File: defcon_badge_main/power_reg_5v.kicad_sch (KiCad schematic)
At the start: 6 parts, among them U2 TPS61023DRLR

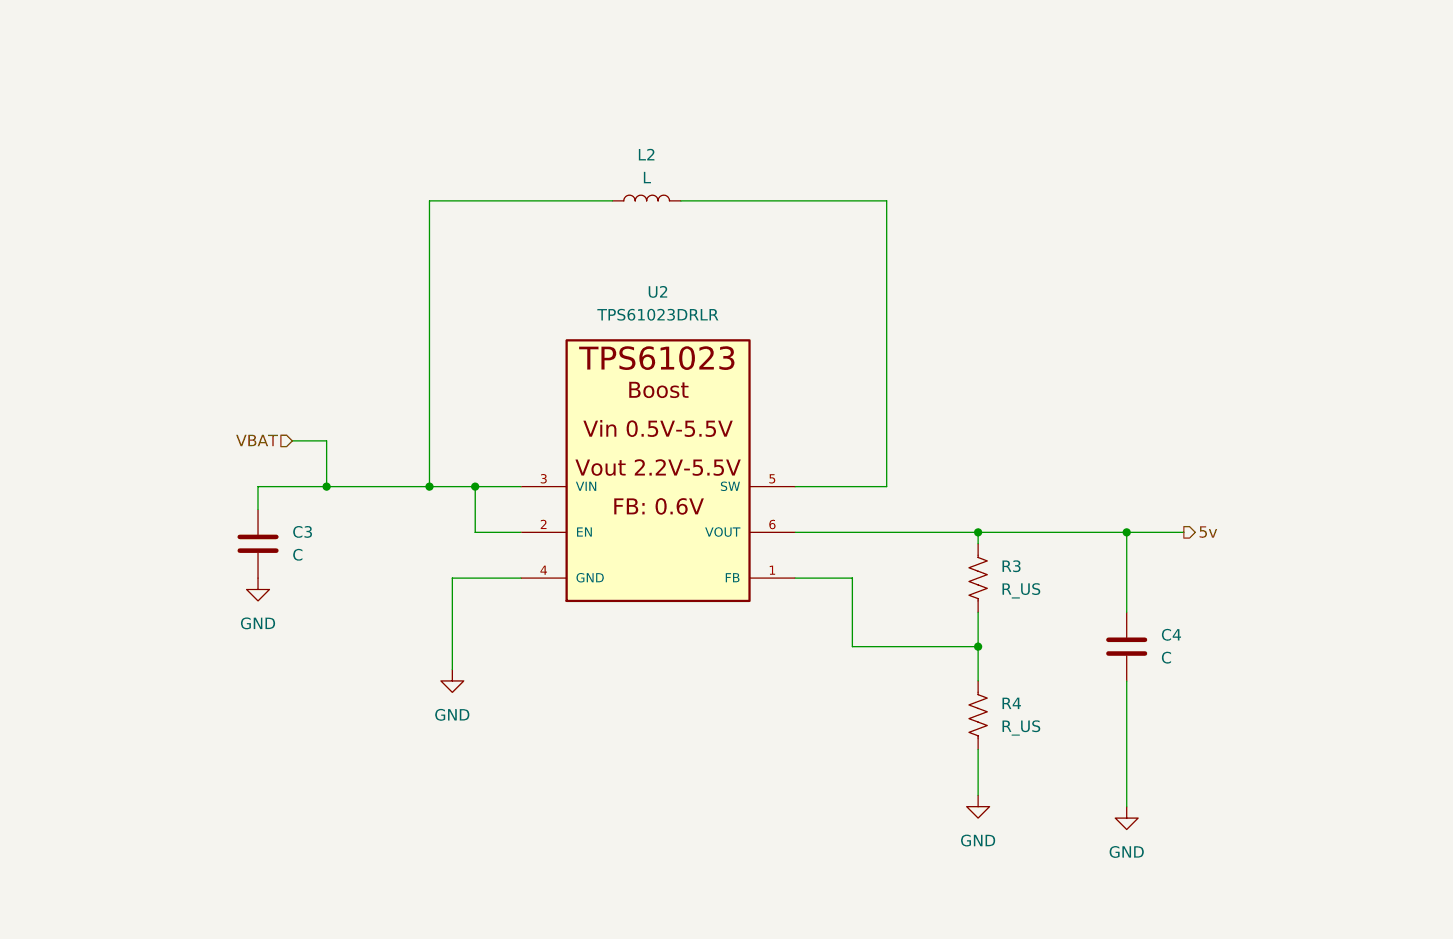
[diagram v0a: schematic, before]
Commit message: ESP32 test board layout
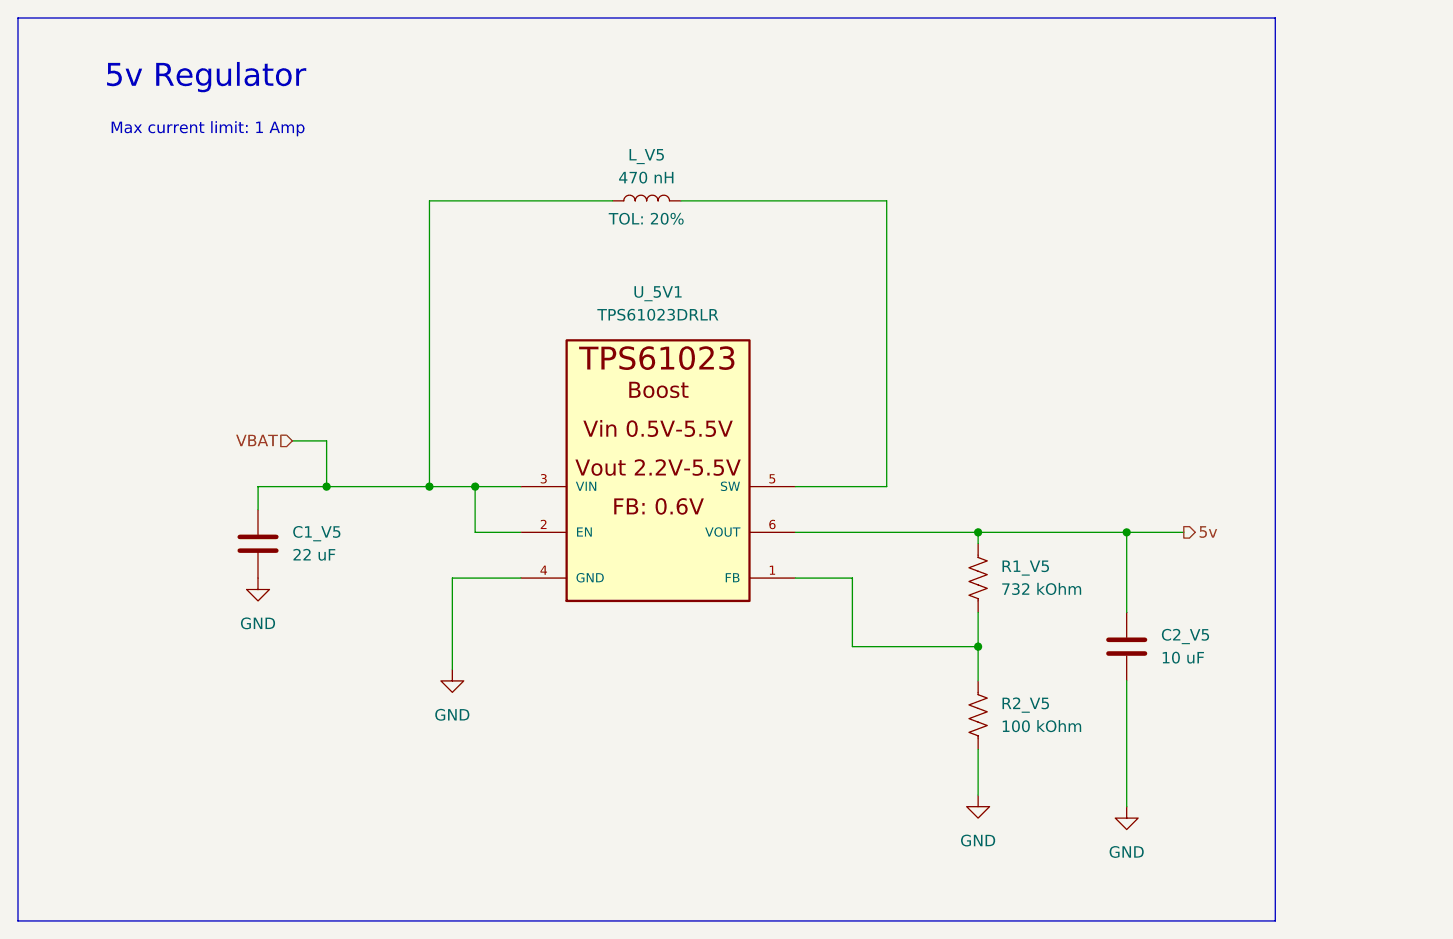
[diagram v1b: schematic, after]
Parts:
- removed L2: L, symbol Device:L
- removed U2: TPS61023DRLR, TPS61023DRLR:SOT563-ORI, symbol TPS61023DRLR:TPS61023DRLR
- added L_V5: 470 nH, Inductor_SMD:L_Neosid_SMS-ME3010, symbol Device:L
- added U_5V1: TPS61023DRLR, TPS61023DRLR:SOT563-ORI, symbol TPS61023DRLR:TPS61023DRLR
- C1_V5: renamed from C3; value C -> 22 uF; footprint (none) -> PCM_SparkFun-Coil:0805
- C2_V5: renamed from C4; value C -> 10 uF; footprint (none) -> PCM_SparkFun-Coil:0805
- R1_V5: renamed from R3; value R_US -> 732 kOhm; footprint (none) -> PCM_SparkFun-Fuse:1206
- R2_V5: renamed from R4; value R_US -> 100 kOhm; footprint (none) -> PCM_SparkFun-Fuse:1206
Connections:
- net 5v: now also U_5V1.6 (VOUT)
- net GND: now also U_5V1.4 (GND)
- net VBAT: now also L_V5.1, U_5V1.2 (EN), U_5V1.3 (VIN)
- net at R1_V5.2, R2_V5.1: now also U_5V1.1 (FB)
- new net: L_V5.2, U_5V1.5 (SW)
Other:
- note added: "5v Regulator"
- note added: "Max current limit: 1 Amp"
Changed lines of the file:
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@@
 	(generator_version "9.0")
 	(paper "A4")
+	(rectangle
+		(start 46.99 29.21)
+		(end 186.69 129.54)
+		(stroke
+			(width 0)
+			(type default)
+		)
+		(fill
+			(type none)
+		)
+	)
+	(text "Max current limit: 1 Amp"
+		(exclude_from_sim no)
+		(at 68.072 41.656 0)
+		(effects
+			(font
+				(size 1.27 1.27)
+			)
+		)
+	)
+	(text "5v Regulator"
+		(exclude_from_sim no)
+		(at 67.818 35.814 0)
+		(effects
+			(font
+				(size 2.54 2.54)
+			)
+		)
+	)
 	(junction
 		(at 97.79 81.28)
@@
 		(dnp no)
 		(fields_autoplaced yes)
-		(property "Reference" "C3"
+		(property "Reference" "C1_V5"
 			(at 77.47 86.3599 0)
 			(effects
@@
 			)
 		)
-		(property "Value" "C"
+		(property "Value" "22 uF"
 			(at 77.47 88.8999 0)
 			(effects
@@
 			)
 		)
-		(property "Footprint" ""
+		(property "Footprint" "PCM_SparkFun-Coil:0805"
 			(at 74.6252 91.44 0)
 			(effects
@@
 			(project "defcon_badge_main"
 				(path "/b497f1e3-23b9-4176-bc4d-bc3995ba532c/5a5d7d00-ae35-4e4f-8d3e-dea7a6dc9222"
-					(reference "C3")
+					(reference "C1_V5")
 					(unit 1)
 				)
@@
 		(dnp no)
 		(fields_autoplaced yes)
-		(property "Reference" "C4"
+		(property "Reference" "C2_V5"
 			(at 173.99 97.7899 0)
 			(effects
@@
 			)
 		)
-		(property "Value" "C"
+		(property "Value" "10 uF"
 			(at 173.99 100.3299 0)
 			(effects
@@
 			)
 		)
-		(property "Footprint" ""
+		(property "Footprint" "PCM_SparkFun-Coil:0805"
 			(at 171.1452 102.87 0)
 			(effects
@@
 			(project "defcon_badge_main"
 				(path "/b497f1e3-23b9-4176-bc4d-bc3995ba532c/5a5d7d00-ae35-4e4f-8d3e-dea7a6dc9222"
-					(reference "C4")
+					(reference "C2_V5")
 					(unit 1)
 				)
@@
 		(on_board yes)
 		(dnp no)
-		(fields_autoplaced yes)
-		(property "Reference" "L2"
+		(property "Reference" "L_V5"
 			(at 116.84 44.45 90)
 			(effects
@@
 			)
 		)
-		(property "Value" "L"
+		(property "Value" "470 nH"
 			(at 116.84 46.99 90)
 			(effects
@@
 			)
 		)
-		(property "Footprint" ""
+		(property "Footprint" "Inductor_SMD:L_Neosid_SMS-ME3010"
 			(at 116.84 49.53 0)
 			(effects
@@
 				)
 				(hide yes)
+			)
+		)
+		(property "PN" "74479288147"
+			(at 116.84 49.53 90)
+			(effects
+				(font
+					(size 1.27 1.27)
+				)
+				(hide yes)
+			)
+		)
+		(property "TOL" "20%"
+			(at 116.84 51.562 90)
+			(show_name yes)
+			(effects
+				(font
+					(size 1.27 1.27)
+				)
 			)
 		)
@@
 			(project "defcon_badge_main"
 				(path "/b497f1e3-23b9-4176-bc4d-bc3995ba532c/5a5d7d00-ae35-4e4f-8d3e-dea7a6dc9222"
-					(reference "L2")
+					(reference "L_V5")
 					(unit 1)
 				)
@@
 		(dnp no)
 		(fields_autoplaced yes)
-		(property "Reference" "R4"
+		(property "Reference" "R2_V5"
 			(at 156.21 105.4099 0)
 			(effects
@@
 			)
 		)
-		(property "Value" "R_US"
+		(property "Value" "100 kOhm"
 			(at 156.21 107.9499 0)
 			(effects
@@
 			)
 		)
-		(property "Footprint" ""
+		(property "Footprint" "PCM_SparkFun-Fuse:1206"
 			(at 154.686 106.934 90)
 			(effects
@@
 			(project "defcon_badge_main"
 				(path "/b497f1e3-23b9-4176-bc4d-bc3995ba532c/5a5d7d00-ae35-4e4f-8d3e-dea7a6dc9222"
-					(reference "R4")
+					(reference "R2_V5")
 					(unit 1)
 				)
@@
 		(dnp no)
 		(fields_autoplaced yes)
-		(property "Reference" "R3"
+		(property "Reference" "R1_V5"
 			(at 156.21 90.1699 0)
 			(effects
@@
 			)
 		)
-		(property "Value" "R_US"
+		(property "Value" "732 kOhm"
 			(at 156.21 92.7099 0)
 			(effects
@@
 			)
 		)
-		(property "Footprint" ""
+		(property "Footprint" "PCM_SparkFun-Fuse:1206"
 			(at 154.686 91.694 90)
 			(effects
@@
 			(project "defcon_badge_main"
 				(path "/b497f1e3-23b9-4176-bc4d-bc3995ba532c/5a5d7d00-ae35-4e4f-8d3e-dea7a6dc9222"
-					(reference "R3")
+					(reference "R1_V5")
 					(unit 1)
 				)
@@
 		(dnp no)
 		(fields_autoplaced yes)
-		(property "Reference" "U2"
+		(property "Reference" "U_5V1"
 			(at 118.11 59.69 0)
 			(effects
@@
 			)
 		)
+		(pin "2"
+		)
+		(pin "5"
+		)
 		(pin "4"
 		)
-		(pin "5"
-		)
 		(pin "6"
 		)
-		(pin "2"
-		)
 		(pin "1"
 		)
@@
 		)
 		(instances
-			(project "defcon_badge_main"
+			(project ""
 				(path "/b497f1e3-23b9-4176-bc4d-bc3995ba532c/5a5d7d00-ae35-4e4f-8d3e-dea7a6dc9222"
-					(reference "U2")
+					(reference "U_5V1")
 					(unit 1)
 				)

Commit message: more layout
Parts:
- C1_V5, C2_V5: footprint PCM_SparkFun-Coil:0805 -> joystick:R_0805_2012Metric_Pad1.20x1.40mm_HandSolder_MINE
- R1_V5, R2_V5: footprint PCM_SparkFun-Fuse:1206 -> joystick:R_1206_3216Metric_Pad1.30x1.75mm_HandSolder_MINE
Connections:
- net 5v_SW: now reaches L_V5.2, U_5V1.5 (SW)
- net 5v_FB: now reaches R1_V5.2, R2_V5.1, U_5V1.1 (FB)
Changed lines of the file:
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@@
+		)
+	)
+	(label "5v_SW"
+		(at 143.51 73.66 0)
+		(effects
+			(font
+				(size 1.27 1.27)
+			)
+			(justify left bottom)
+		)
+	)
+	(label "5v_FB"
+		(at 143.51 99.06 0)
+		(effects
+			(font
+				(size 1.27 1.27)
+			)
+			(justify left bottom)
 		)
 	)
@@
 			)
 		)
-		(property "Footprint" "PCM_SparkFun-Coil:0805"
+		(property "Footprint" "joystick:R_0805_2012Metric_Pad1.20x1.40mm_HandSolder_MINE"
 			(at 74.6252 91.44 0)
 			(effects
@@
 			)
 		)
-		(property "Footprint" "PCM_SparkFun-Coil:0805"
+		(property "Footprint" "joystick:R_0805_2012Metric_Pad1.20x1.40mm_HandSolder_MINE"
 			(at 171.1452 102.87 0)
 			(effects
@@
 			)
 		)
-		(property "Footprint" "PCM_SparkFun-Fuse:1206"
+		(property "Footprint" "joystick:R_1206_3216Metric_Pad1.30x1.75mm_HandSolder_MINE"
 			(at 154.686 106.934 90)
 			(effects
@@
 			)
 		)
-		(property "Footprint" "PCM_SparkFun-Fuse:1206"
+		(property "Footprint" "joystick:R_1206_3216Metric_Pad1.30x1.75mm_HandSolder_MINE"
 			(at 154.686 91.694 90)
 			(effects

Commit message: moar layout
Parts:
- added D_8V2: SS24FL, SS24FL:SODFL3617X108N, symbol SS24FL:SS24FL
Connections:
- net 5v: now also D_8V2.C; no longer C2_V5.1, R1_V5.1, U_5V1.6 (VOUT)
- new net 5v_out: C2_V5.1, D_8V2.A, R1_V5.1, U_5V1.6 (VOUT)
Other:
- note added: "Need to prevent USB 5v Power current backflow when connected to host"
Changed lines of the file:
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@@
 	(rectangle
 		(start 46.99 29.21)
-		(end 186.69 129.54)
+		(end 204.47 129.54)
 		(stroke
 			(width 0)
@@
 		)
 	)
+	(text "Need to prevent USB 5v Power \ncurrent backflow when connected to host"
+		(exclude_from_sim no)
+		(at 172.466 55.118 0)
+		(effects
+			(font
+				(size 1.27 1.27)
+			)
+		)
+	)
 	(text "5v Regulator"
 		(exclude_from_sim no)
@@
 		)
 	)
-	(hierarchical_label "5v"
-		(shape output)
-		(at 176.53 86.36 0)
+	(label "5v_out"
+		(at 157.48 86.36 0)
 		(effects
 			(font
 				(size 1.27 1.27)
 			)
-			(justify left)
+			(justify left bottom)
 		)
 	)
@@
 			)
 			(justify right)
+		)
+	)
+	(hierarchical_label "5v"
+		(shape output)
+		(at 186.69 86.36 0)
+		(effects
+			(font
+				(size 1.27 1.27)
+			)
+			(justify left)
 		)
 	)
@@
 					(unit 1)
 				)
+			)
+		)
+	)
+	(symbol
+		(lib_id "SS24FL:SS24FL")
+		(at 181.61 86.36 0)
+		(unit 1)
+		(exclude_from_sim no)
+		(in_bom yes)
+		(on_board yes)
+		(dnp no)
+		(fields_autoplaced yes)
+		(property "Reference" "D_8V2"
+			(at 181.61 80.01 0)
+			(effects
+				(font
+					(size 1.27 1.27)
+				)
+			)
+		)
+		(property "Value" "SS24FL"
+			(at 181.61 82.55 0)
+			(effects
+				(font
+					(size 1.27 1.27)
+				)
+			)
+		)
+		(property "Footprint" "SS24FL:SODFL3617X108N"
+			(at 181.61 86.36 0)
+			(effects
+				(font
+					(size 1.27 1.27)
+				)
+				(justify bottom)
+				(hide yes)
+			)
+		)
+		(property "Datasheet" ""
+			(at 181.61 86.36 0)
+			(effects
+				(font
+					(size 1.27 1.27)
+				)
+				(hide yes)
+			)
+		)
+		(property "Description" ""
+			(at 181.61 86.36 0)
+			(effects
+				(font
+					(size 1.27 1.27)
+				)
+				(hide yes)
+			)
+		)
+		(property "MF" "ON Semiconductor"
+			(at 181.61 86.36 0)
+			(effects
+				(font
+					(size 1.27 1.27)
+				)
+				(justify bottom)
+				(hide yes)
+			)
+		)
+		(property "MAXIMUM_PACKAGE_HEIGHT" "1.08mm"
+			(at 181.61 86.36 0)
+			(effects
+				(font
+					(size 1.27 1.27)
+				)
+				(justify bottom)
+				(hide yes)
+			)
+		)
+		(property "Package" "SOD-123F ON Semiconductor"
+			(at 181.61 86.36 0)
+			(effects
+				(font
+					(size 1.27 1.27)
+				)
+				(justify bottom)
+				(hide yes)
+			)
+		)
+		(property "Price" "None"
+			(at 181.61 86.36 0)
+			(effects
+				(font
+					(size 1.27 1.27)
+				)
+				(justify bottom)
+				(hide yes)
+			)
+		)
+		(property "Check_prices" "https://www.snapeda.com/parts/SS24FL/Onsemi/view-part/?ref=eda"
+			(at 181.61 86.36 0)
+			(effects
+				(font
+					(size 1.27 1.27)
+				)
+				(justify bottom)
+				(hide yes)
+			)
+		)
+		(property "STANDARD" "IPC-7351B"
+			(at 181.61 86.36 0)
+			(effects
+				(font
+					(size 1.27 1.27)
+				)
+				(justify bottom)
+				(hide yes)
+			)
+		)
+		(property "PARTREV" "A"
+			(at 181.61 86.36 0)
+			(effects
+				(font
+					(size 1.27 1.27)
+				)
+				(justify bottom)
+				(hide yes)
+			)
+		)
+		(property "SnapEDA_Link" "https://www.snapeda.com/parts/SS24FL/Onsemi/view-part/?ref=snap"
+			(at 181.61 86.36 0)
+			(effects
+				(font
+					(size 1.27 1.27)
+				)
+				(justify bottom)
+				(hide yes)
+			)
+		)
+		(property "MP" "SS24FL"
+			(at 181.61 86.36 0)
+			(effects
+				(font
+					(size 1.27 1.27)
+				)
+				(justify bottom)
+				(hide yes)
+			)
+		)
+		(property "Description_1" "Diode Schottky 40 V 2A Surface Mount SOD-123F"
+			(at 181.61 86.36 0)
+			(effects
+				(font
+					(size 1.27 1.27)
+				)
+				(justify bottom)
+				(hide yes)
+			)
+		)
+		(property "Availability" "In Stock"
+			(at 181.61 86.36 0)
+			(effects
+				(font
+					(size 1.27 1.27)
+				)
+				(justify bottom)
+				(hide yes)
+			)
+		)
+		(property "MANUFACTURER" "ON Semiconductor"
+			(at 181.61 86.36 0)
+			(effects
+				(font
+					(size 1.27 1.27)
+				)
+				(justify bottom)
+				(hide yes)
+			)
+		)
+		(pin "C"
+		)
+		(pin "A"
+		)
+		(instances
+			(project "defcon_badge_main"
+				(path "/b497f1e3-23b9-4176-bc4d-bc3995ba532c/5a5d7d00-ae35-4e4f-8d3e-dea7a6dc9222"
+					(reference "D_8V2")
+					(unit 1)
+				)

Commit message: added component parts and modifications
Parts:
- C1_V5: MPN (none) -> GMC21X5R226K16NT; Rating (none) -> 16V
- C2_V5: MPN (none) -> GMC21X5R106K16NT; Rating (none) -> 16V
- D_8V2: MPN (none) -> SS24FL
- L_V5: MPN (none) -> 74479288147
- R1_V5: MPN (none) -> RM12F7323CT; TOL (none) -> 1%
- R2_V5: MPN (none) -> RM12F1003CT; TOL (none) -> 1%
- U_5V1: MPN (none) -> TPS61023DRLR
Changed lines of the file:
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@@
 			)
 		)
-		(property "Datasheet" "~"
+		(property "Datasheet" "~https://calchip.com/wp-content/uploads/2025/05/GMC-Series-3.pdf"
 			(at 73.66 87.63 0)
 			(effects
@@
 		)
 		(property "Description" "Unpolarized capacitor"
+			(at 73.66 87.63 0)
+			(effects
+				(font
+					(size 1.27 1.27)
+				)
+				(hide yes)
+			)
+		)
+		(property "MPN" "GMC21X5R226K16NT"
+			(at 73.66 87.63 0)
+			(effects
+				(font
+					(size 1.27 1.27)
+				)
+				(hide yes)
+			)
+		)
+		(property "Rating" "16V"
 			(at 73.66 87.63 0)
 			(effects
@@
 			)
 		)
-		(property "Datasheet" "~"
+		(property "Datasheet" "https://calchip.com/wp-content/uploads/2025/05/GMC-Series-3.pdf"
 			(at 170.18 99.06 0)
 			(effects
@@
 		)
 		(property "Description" "Unpolarized capacitor"
+			(at 170.18 99.06 0)
+			(effects
+				(font
+					(size 1.27 1.27)
+				)
+				(hide yes)
+			)
+		)
+		(property "MPN" "GMC21X5R106K16NT"
+			(at 170.18 99.06 0)
+			(effects
+				(font
+					(size 1.27 1.27)
+				)
+				(hide yes)
+			)
+		)
+		(property "Rating" "16V"
 			(at 170.18 99.06 0)
 			(effects
@@
 			)
 		)
-		(property "Datasheet" "~"
+		(property "Datasheet" "https://www.we-online.com/components/products/datasheet/74479288147.pdf"
 			(at 116.84 49.53 0)
 			(effects
@@
 					(size 1.27 1.27)
 				)
+			)
+		)
+		(property "MPN" "74479288147"
+			(at 116.84 49.53 90)
+			(effects
+				(font
+					(size 1.27 1.27)
+				)
+				(hide yes)
 			)
 		)
@@
 			)
 		)
-		(property "Datasheet" "~"
+		(property "Datasheet" "https://calchip.com/wp-content/uploads/2025/05/RMSERIES-052225.pdf"
 			(at 153.67 106.68 0)
 			(effects
@@
 		)
 		(property "Description" "Resistor, US symbol"
+			(at 153.67 106.68 0)
+			(effects
+				(font
+					(size 1.27 1.27)
+				)
+				(hide yes)
+			)
+		)
+		(property "MPN" "RM12F1003CT"
+			(at 153.67 106.68 0)
+			(effects
+				(font
+					(size 1.27 1.27)
+				)
+				(hide yes)
+			)
+		)
+		(property "TOL" "1%"
 			(at 153.67 106.68 0)
 			(effects
@@
 			)
 		)
-		(property "Datasheet" "~"
+		(property "Datasheet" "https://calchip.com/wp-content/uploads/2025/05/RMSERIES-052225.pdf"
 			(at 153.67 91.44 0)
 			(effects
@@
 		)
 		(property "Description" "Resistor, US symbol"
+			(at 153.67 91.44 0)
+			(effects
+				(font
+					(size 1.27 1.27)
+				)
+				(hide yes)
+			)
+		)
+		(property "MPN" "RM12F7323CT"
+			(at 153.67 91.44 0)
+			(effects
+				(font
+					(size 1.27 1.27)
+				)
+				(hide yes)
+			)
+		)
+		(property "TOL" "1%"
 			(at 153.67 91.44 0)
 			(effects
@@
 			)
 		)
-		(property "Datasheet" ""
+		(property "Datasheet" "https://www.ti.com/lit/ds/symlink/tps61023.pdf?HQS=dis-dk-null-digikeymode-dsf-pf-null-wwe&ts=1777151769302&ref_url=https%253A%252F%252Fwww.ti.com%252Fgeneral%252Fdocs%252Fsuppproductinfo.tsp%253FdistId%253D10%2526gotoUrl%253Dhttps%253A%252F%252Fwww.ti.com%252Flit%252Fgpn%252Ftps61023"
 			(at 118.11 86.36 0)
 			(effects
@@
 				)
 				(justify bottom)
+				(hide yes)
+			)
+		)
+		(property "MPN" "TPS61023DRLR"
+			(at 118.11 86.36 0)
+			(effects
+				(font
+					(size 1.27 1.27)
+				)
 				(hide yes)
 			)
@@
 			)
 		)
-		(property "Datasheet" ""
+		(property "Datasheet" "https://www.onsemi.com/pdf/datasheet/ss26fl-d.pdf"
 			(at 181.61 86.36 0)
 			(effects
@@
 				(hide yes)
 			)
+		)
+		(property "MPN" "SS24FL"
+			(at 181.61 86.36 0)
+			(effects
+				(font
+					(size 1.27 1.27)
+				)
+				(hide yes)
+			)
